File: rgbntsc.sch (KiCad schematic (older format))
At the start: 37 parts, among them J1 VGA, J2 Mini-DIN-4, J3 USB_C_Receptacle_Power, J4 SCART_CONN, U1 SC6206B-65K5, U2 AD724, U8 LM1881, X1 ASE-14.32MHz

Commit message: CXA2075
Replaces AD724 with CXA2075, also adds GBS compatible RGB out header
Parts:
- removed C13, C14: 100n, Capacitor_SMD:C_0805_2012Metric_Pad1.15x1.40mm_HandSolder, symbol Device:C_Small
- removed C3: 1u, Capacitor_SMD:C_0805_2012Metric_Pad1.15x1.40mm_HandSolder, symbol Device:C_Small
- removed C9: 10u, Capacitor_SMD:C_0805_2012Metric_Pad1.15x1.40mm_HandSolder, symbol Device:C_Small
- removed J3: USB_C_Receptacle_Power, videobits:USB_C_Receptacle_Generic_Power_Only, symbol Videobits:USB_C_Receptacle_Power
- removed J4: SCART_CONN, custom_components:SCART_CONN, symbol ossc:SCART_CONN
- removed JP1: Jumper_2_Open, Resistor_SMD:R_0805_2012Metric_Pad1.15x1.40mm_HandSolder, symbol Jumper:Jumper_2_Open
- removed R15, R3: 75, Resistor_SMD:R_0805_2012Metric_Pad1.15x1.40mm_HandSolder, symbol Device:R_Small
- removed R18: 680k, Resistor_SMD:R_0805_2012Metric_Pad1.15x1.40mm_HandSolder, symbol Device:R_Small
- removed R19, R2: 1k, Resistor_SMD:R_0805_2012Metric_Pad1.15x1.40mm_HandSolder, symbol Device:R_Small
- removed U1: SC6206B-65K5, Package_TO_SOT_SMD:SOT-23, symbol Regulator_Linear:MCP1700-2802E_SOT23
- removed U2: AD724, Package_SO:SOIC-16W_7.5x10.3mm_P1.27mm, symbol rgbntsc-rescue:AD724-Videobits
- added C1: 100n, Capacitor_SMD:C_0805_2012Metric_Pad1.15x1.40mm_HandSolder, symbol Device:C_Small
- added C11: 10u, Capacitor_SMD:C_0805_2012Metric_Pad1.15x1.40mm_HandSolder, symbol Device:C_Small
- added C7, C8: 1u, Capacitor_SMD:C_0805_2012Metric_Pad1.15x1.40mm_HandSolder, symbol Device:C_Small
- added J1: USB_C_Receptacle_Power, videobits:USB_C_Receptacle_Generic_Power_Only, symbol Videobits:USB_C_Receptacle_Power
- added J101: Conn_01x08, Connector_JST:JST_XH_B8B-XH-AM_1x08_P2.50mm_Vertical, symbol Connector_Generic:Conn_01x08
- added J3: SCART_CONN, custom_components:SCART_CONN, symbol ossc:SCART_CONN
- added JP101: Jumper_3_Bridged12, Jumper:SolderJumper-3_P1.3mm_Bridged12_Pad1.0x1.5mm, symbol Jumper:Jumper_3_Bridged12
- added R101, R103, R104, R6, R7: 75, Resistor_SMD:R_0805_2012Metric_Pad1.15x1.40mm_HandSolder, symbol Device:R_Small
- added R102, R9: 1k, Resistor_SMD:R_0805_2012Metric_Pad1.15x1.40mm_HandSolder, symbol Device:R_Small
- added R11: 3k3, Resistor_SMD:R_0805_2012Metric_Pad1.15x1.40mm_HandSolder, symbol Device:R_Small
- added R8: 3k, Resistor_SMD:R_0805_2012Metric_Pad1.15x1.40mm_HandSolder, symbol Device:R_Small
- added U102, U103: 74AHCT1G86, Package_TO_SOT_SMD:SOT-23-5, symbol 74xGxx:74AHC1G86
- added U2: SC6206B-65K5, Package_TO_SOT_SMD:SOT-23, symbol Regulator_Linear:MCP1700-2802E_SOT23
- added U3: CXA2075, Package_SO:SOP-24_7.5x15.4mm_P1.27mm, symbol Videobits:CXA2075
- C2: value 1u -> 100n; LCSC C28323 -> C49678
- C3: renamed from C8; LCSC C14663 -> C49678
- C4: renamed from C10; LCSC C14663 -> C49678
- C5: renamed from C4; LCSC C14663 -> C49678
- C9: renamed from C11; LCSC C14663 -> C49678
- R1: value 3k -> 75; LCSC C17513 -> C20638
- R4: value 75 -> 680k; LCSC C20638 -> C17797
- X1: value ASE-14.32MHz -> O32253579545MHEA4SI; LCSC C295523 -> C70606
- renumbered C7 to C10, C1 to C6, J1 to J2, J2 to J4, R5 to R10, R6 to R12, R7 to R13, R8 to R14, R16 to R2, R17 to R3, U8 to U1
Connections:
- net labels added: STRIP_CSYNC, SYNC, VGA_CSYNC
- wire segments 113 -> 146

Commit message: added 1v amp and output caps
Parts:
- removed J101: Conn_01x08, Connector_JST:JST_XH_B8B-XH-AM_1x08_P2.50mm_Vertical, symbol Connector_Generic:Conn_01x08
- removed R101, R103, R104: 75, Resistor_SMD:R_0805_2012Metric_Pad1.15x1.40mm_HandSolder, symbol Device:R_Small
- added C12, C13, C14: 220u, Capacitor_SMD:CP_Elec_6.3x5.4, symbol Device:CP_Small
- added C15, C16, C17: 1u, Capacitor_SMD:C_0805_2012Metric, symbol rgbntsc-rescue:C_Small-Device
- added R15, R16, R17: 180, Resistor_SMD:R_0805_2012Metric, symbol rgbntsc-rescue:R_Small-Device
- added R18, R19, R20: 75, Resistor_SMD:R_0805_2012Metric, symbol rgbntsc-rescue:R_Small-Device
- added U6: TPF144-VR, Package_SO:MSOP-10_3x3mm_P0.5mm, symbol Videobits:TPF144-VR
- C1, C2, C3, C4: footprint Capacitor_SMD:C_0805_2012Metric_Pad1.15x1.40mm_HandSolder -> Capacitor_SMD:C_0805_2012Metric; symbol Device:C_Small -> rgbntsc-rescue:C_Small-Device
- C10: renamed from C11; footprint Capacitor_SMD:C_0805_2012Metric_Pad1.15x1.40mm_HandSolder -> Capacitor_SMD:C_0805_2012Metric; symbol Device:C_Small -> rgbntsc-rescue:C_Small-Device
- C11: renamed from C5; footprint Capacitor_SMD:C_0805_2012Metric_Pad1.15x1.40mm_HandSolder -> Capacitor_SMD:C_0805_2012Metric; symbol Device:C_Small -> rgbntsc-rescue:C_Small-Device
- C5: renamed from C6; footprint Capacitor_SMD:C_0805_2012Metric_Pad1.15x1.40mm_HandSolder -> Capacitor_SMD:C_0805_2012Metric; symbol Device:C_Small -> rgbntsc-rescue:C_Small-Device
- C6: renamed from C7; footprint Capacitor_SMD:C_0805_2012Metric_Pad1.15x1.40mm_HandSolder -> Capacitor_SMD:C_0805_2012Metric; symbol Device:C_Small -> rgbntsc-rescue:C_Small-Device
- C7: renamed from C8; footprint Capacitor_SMD:C_0805_2012Metric_Pad1.15x1.40mm_HandSolder -> Capacitor_SMD:C_0805_2012Metric; symbol Device:C_Small -> rgbntsc-rescue:C_Small-Device
- C8: renamed from C9; footprint Capacitor_SMD:C_0805_2012Metric_Pad1.15x1.40mm_HandSolder -> Capacitor_SMD:C_0805_2012Metric; symbol Device:C_Small -> rgbntsc-rescue:C_Small-Device
- C9: renamed from C10; symbol Device:CP_Small -> rgbntsc-rescue:CP_Small-Device
- GOTE1: symbol Mechanical:Fiducial -> rgbntsc-rescue:Fiducial-Mechanical
- J4: symbol Connector:Mini-DIN-4 -> rgbntsc-rescue:Mini-DIN-4-Connector
- JP1: renamed from JP101; symbol Jumper:Jumper_3_Bridged12 -> rgbntsc-rescue:Jumper_3_Bridged12-Jumper
- JR1, JR2, JU1: symbol Connector:Conn_Coaxial -> rgbntsc-rescue:Conn_Coaxial-Connector
- R1, R10, R11, R12, R13, R14, R2, R3, R4, R6, R7: footprint Resistor_SMD:R_0805_2012Metric_Pad1.15x1.40mm_HandSolder -> Resistor_SMD:R_0805_2012Metric; symbol Device:R_Small -> rgbntsc-rescue:R_Small-Device
- R5: renamed from R102; footprint Resistor_SMD:R_0805_2012Metric_Pad1.15x1.40mm_HandSolder -> Resistor_SMD:R_0805_2012Metric; symbol Device:R_Small -> rgbntsc-rescue:R_Small-Device
- R8: value 3k -> 1k; footprint Resistor_SMD:R_0805_2012Metric_Pad1.15x1.40mm_HandSolder -> Resistor_SMD:R_0805_2012Metric; symbol Device:R_Small -> rgbntsc-rescue:R_Small-Device
- R9: value 1k -> 1k3; footprint Resistor_SMD:R_0805_2012Metric_Pad1.15x1.40mm_HandSolder -> Resistor_SMD:R_0805_2012Metric; symbol Device:R_Small -> rgbntsc-rescue:R_Small-Device
- U1: symbol Video:LM1881 -> rgbntsc-rescue:LM1881-Video
- U2: renamed from U102; symbol 74xGxx:74AHC1G86 -> rgbntsc-rescue:74AHC1G86-74xGxx
- U3: renamed from U103; symbol 74xGxx:74AHC1G86 -> rgbntsc-rescue:74AHC1G86-74xGxx
- U4: renamed from U2; symbol Regulator_Linear:MCP1700-2802E_SOT23 -> rgbntsc-rescue:MCP1700-2802E_SOT23-Regulator_Linear
- U5: renamed from U3; footprint Package_SO:SOP-24_7.5x15.4mm_P1.27mm -> Package_SO:SO-24_5.3x15mm_P1.27mm
- X1: symbol Oscillator:ASE-xxxMHz -> rgbntsc-rescue:ASE-xxxMHz-Oscillator
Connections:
- wire segments 146 -> 162
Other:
- moved on the sheet: U5

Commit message: corrected components
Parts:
- C12, C13, C14, U5: LCSC (none) -> NOT FITTED
- R15, R16, R17: LCSC C20638 -> C25270
- R9: LCSC C17513 -> C17384
- U6: LCSC (none) -> C155447
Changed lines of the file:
@@
 F 2 "Resistor_SMD:R_0805_2012Metric" H 5250 6750 50  0001 C CNN
 F 3 "~" H 5250 6750 50  0001 C CNN
-F 4 "C17513" H 5250 6750 50  0001 C CNN "LCSC"
+F 4 "C17384" H 5250 6750 50  0001 C CNN "LCSC"
 	1    5250 6750
 	1    0    0    -1
@@
 F 2 "Package_SO:SO-24_5.3x15mm_P1.27mm" H 7850 2000 60  0001 C CNN
 F 3 "" H 7850 2000 60  0000 C CNN
+F 4 "NOT FITTED" H 7850 2000 50  0001 C CNN "LCSC"
 	1    7850 2000
 	1    0    0    -1
@@
 F 2 "Capacitor_SMD:CP_Elec_6.3x5.4" H 9600 2100 50  0001 C CNN
 F 3 "~" H 9600 2100 50  0001 C CNN
+F 4 "NOT FITTED" H 9600 2100 50  0001 C CNN "LCSC"
 	1    9600 2100
 	0    -1   1    0
@@
 F 2 "Capacitor_SMD:CP_Elec_6.3x5.4" H 9600 2000 50  0001 C CNN
 F 3 "~" H 9600 2000 50  0001 C CNN
+F 4 "NOT FITTED" H 9600 2000 50  0001 C CNN "LCSC"
 	1    9600 2000
 	0    -1   1    0
@@
 F 2 "Capacitor_SMD:CP_Elec_6.3x5.4" H 9600 1900 50  0001 C CNN
 F 3 "~" H 9600 1900 50  0001 C CNN
+F 4 "NOT FITTED" H 9600 1900 50  0001 C CNN "LCSC"
 	1    9600 1900
 	0    -1   1    0
@@
 F 2 "Package_SO:MSOP-10_3x3mm_P0.5mm" H 5475 2797 60  0000 C CNN
 F 3 "" H 5250 2400 60  0000 C CNN
+F 4 "C155447" H 5450 2150 50  0001 C CNN "LCSC"
 	1    5450 2150
 	1    0    0    -1
@@
 F 2 "Resistor_SMD:R_0805_2012Metric" H 7150 2350 50  0001 C CNN
 F 3 "~" H 7150 2350 50  0001 C CNN
-F 4 "C20638" H 7150 2350 50  0001 C CNN "LCSC"
+F 4 "C25270" H 7150 2350 50  0001 C CNN "LCSC"
 	1    7150 2350
 	1    0    0    -1
@@
 F 2 "Resistor_SMD:R_0805_2012Metric" H 7050 2350 50  0001 C CNN
 F 3 "~" H 7050 2350 50  0001 C CNN
-F 4 "C20638" H 7050 2350 50  0001 C CNN "LCSC"
+F 4 "C25270" H 7050 2350 50  0001 C CNN "LCSC"
 	1    7050 2350
 	1    0    0    -1
@@
 F 2 "Resistor_SMD:R_0805_2012Metric" H 6950 2350 50  0001 C CNN
 F 3 "~" H 6950 2350 50  0001 C CNN
-F 4 "C20638" H 6950 2350 50  0001 C CNN "LCSC"
+F 4 "C25270" H 6950 2350 50  0001 C CNN "LCSC"
 	1    6950 2350
 	1    0    0    -1

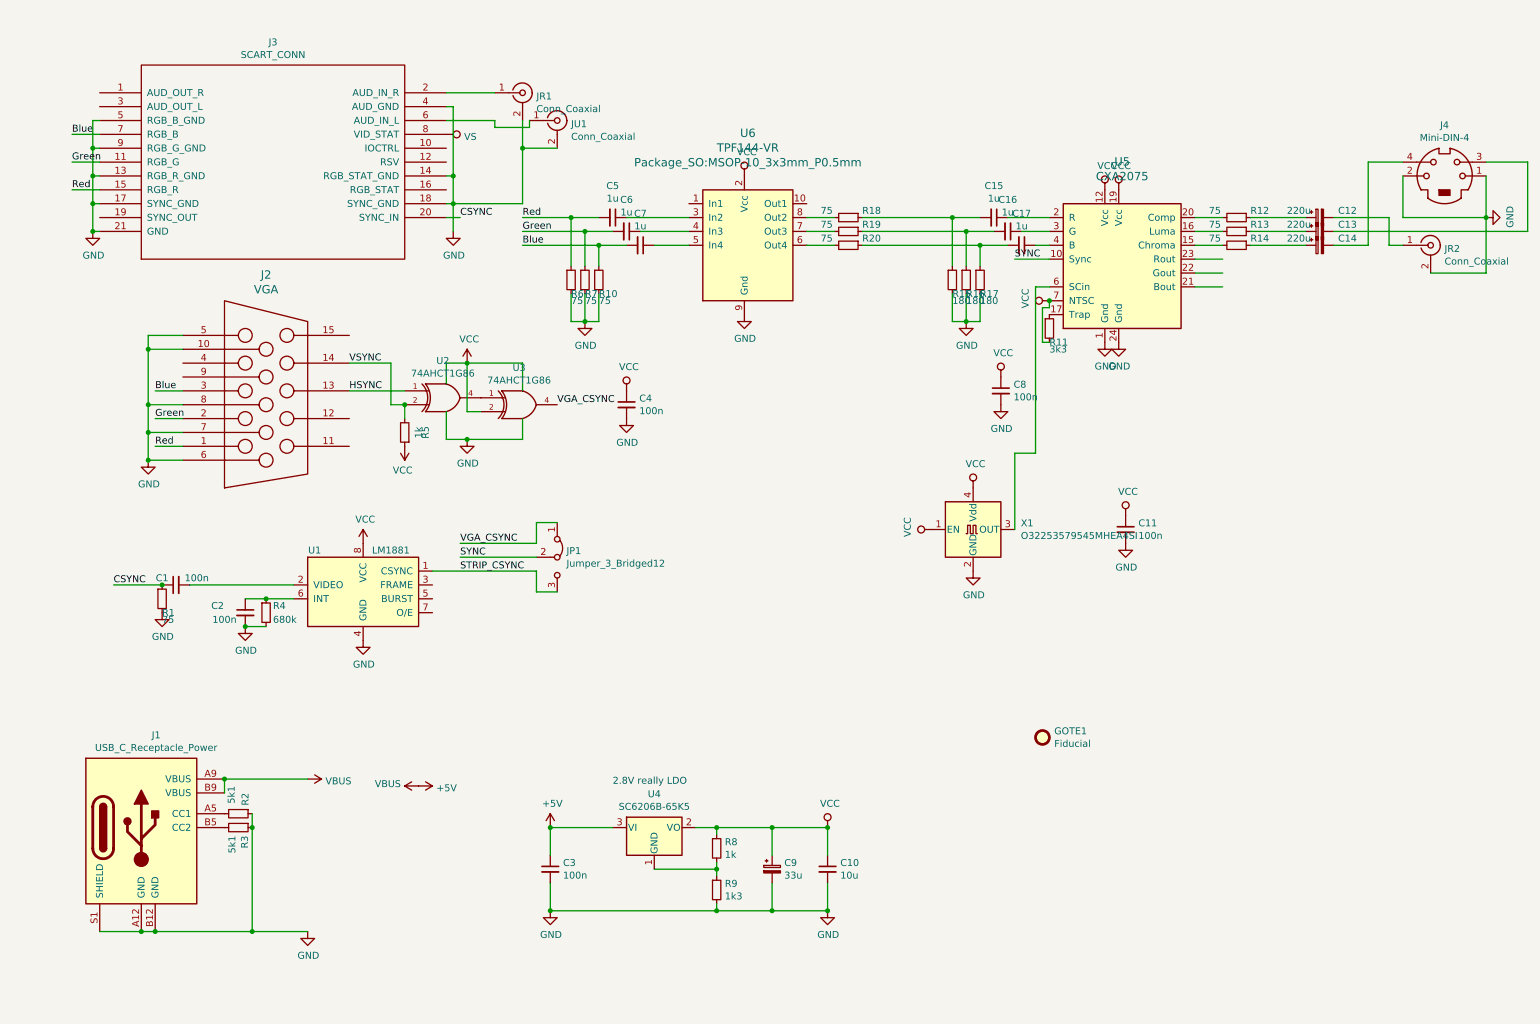
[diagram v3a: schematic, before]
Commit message: add power LED, general tweakage
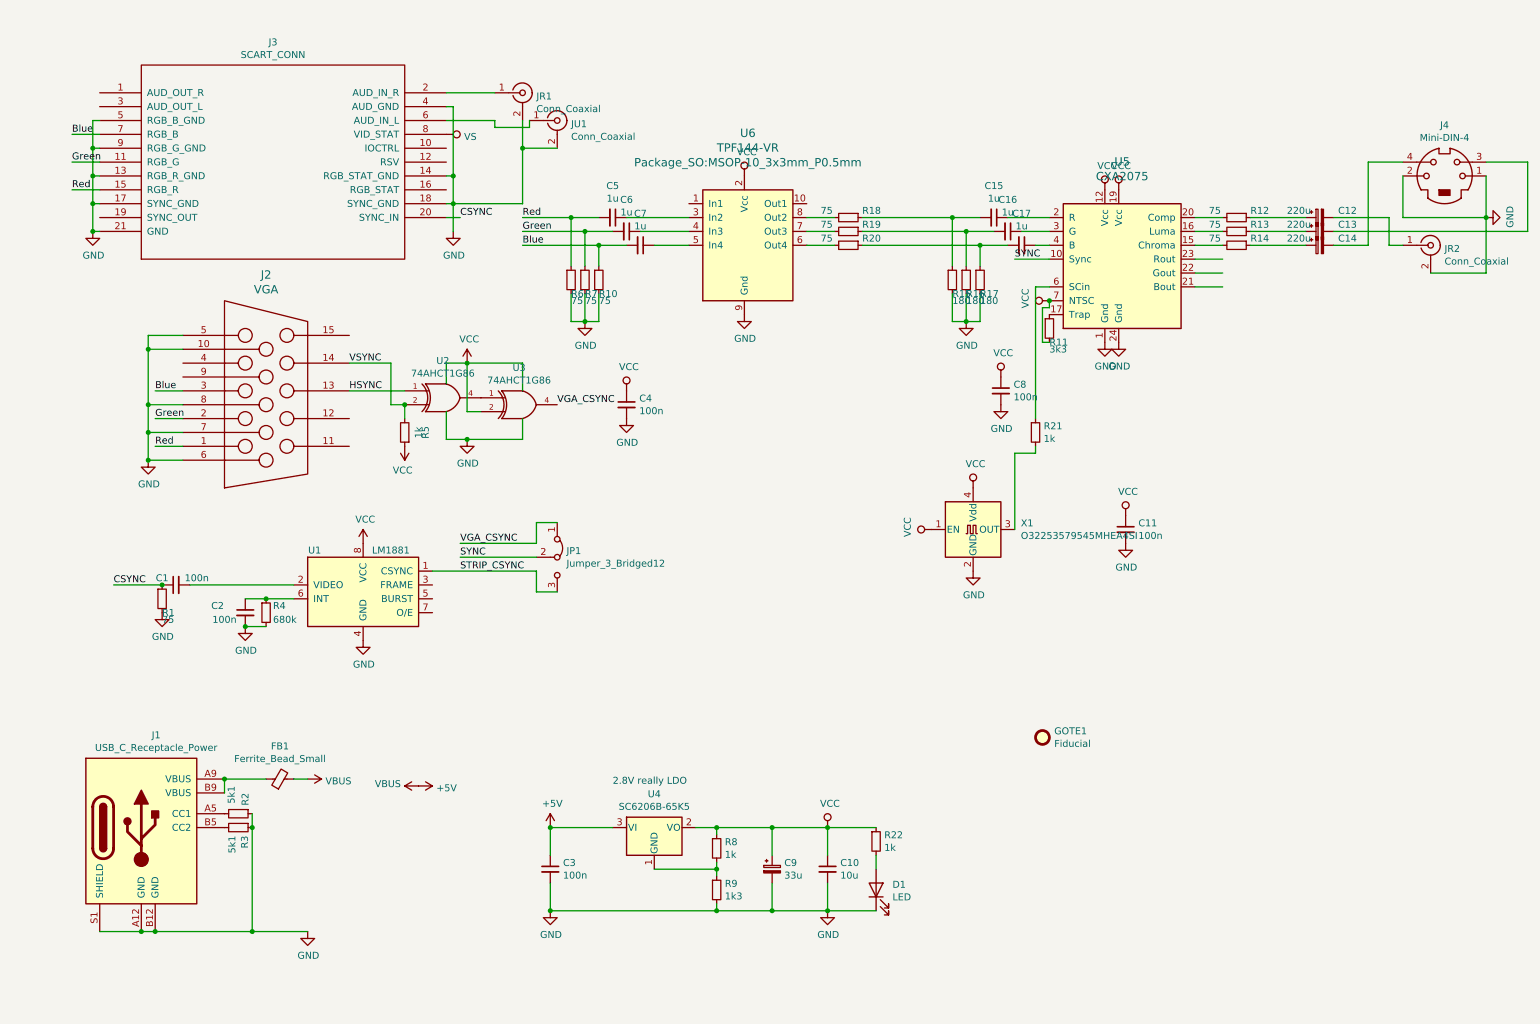
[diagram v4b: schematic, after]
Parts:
- added D1: LED, LED_SMD:LED_0805_2012Metric, symbol Device:LED
- added FB1: Ferrite_Bead_Small, Capacitor_SMD:C_0805_2012Metric, symbol Device:Ferrite_Bead_Small
- added R21, R22: 1k, Resistor_SMD:R_0805_2012Metric, symbol rgbntsc-rescue:R_Small-Device
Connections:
- net +5V: now also FB1.2; no longer J1.A9 (VBUS), J1.B9 (VBUS)
- net GND: now also D1.1 (K)
- net VCC: now also R22.1
- net at X1.3 (OUT): now also R21.2; no longer U5.6 (SCin)
- new net: R21.1, U5.6 (SCin)
- new net: FB1.1, J1.A9 (VBUS), J1.B9 (VBUS)
- new net: D1.2 (A), R22.2
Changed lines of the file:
@@
 	1700 6050 1700 5950
 Wire Wire Line
-	1700 5950 2300 5950
+	1700 5950 2000 5950
 Connection ~ 1700 5950
 $Comp
@@
 	7400 3600 7550 3600
 Wire Wire Line
-	7550 3600 7550 2400
+	7550 3600 7550 3550
 Wire Wire Line
 	7550 2400 7650 2400
@@
 Wire Wire Line
 	7650 2100 7550 2100
+$Comp
+L rgbntsc-rescue:R_Small-Device R21
+U 1 1 60AAAD05
+P 7550 3450
+F 0 "R21" H 7609 3496 50  0000 L CNN
+F 1 "1k" H 7609 3405 50  0000 L CNN
+F 2 "Resistor_SMD:R_0805_2012Metric" H 7550 3450 50  0001 C CNN
+F 3 "~" H 7550 3450 50  0001 C CNN
+F 4 "C17513" H 7550 3450 50  0001 C CNN "LCSC"
+	1    7550 3450
+	1    0    0    -1
+$EndComp
+Wire Wire Line
+	7550 3350 7550 2400
+$Comp
+L Device:Ferrite_Bead_Small FB1
+U 1 1 60AAC928
+P 2100 5950
+F 0 "FB1" V 2337 5950 50  0000 C CNN
+F 1 "Ferrite_Bead_Small" V 2246 5950 50  0000 C CNN
+F 2 "Capacitor_SMD:C_0805_2012Metric" V 2030 5950 50  0001 C CNN
+F 3 "~" H 2100 5950 50  0001 C CNN
+F 4 "C1017" V 2100 5950 50  0001 C CNN "LCSC"
+	1    2100 5950
+	0    -1   -1   0
+$EndComp
+Wire Wire Line
+	2200 5950 2300 5950
+$Comp
+L rgbntsc-rescue:R_Small-Device R22
+U 1 1 60C1454C
+P 6400 6400
+F 0 "R22" H 6459 6446 50  0000 L CNN
+F 1 "1k" H 6459 6355 50  0000 L CNN
+F 2 "Resistor_SMD:R_0805_2012Metric" H 6400 6400 50  0001 C CNN
+F 3 "~" H 6400 6400 50  0001 C CNN
+F 4 "C17513" H 6400 6400 50  0001 C CNN "LCSC"
+	1    6400 6400
+	1    0    0    -1
+$EndComp
+$Comp
+L Device:LED D1
+U 1 1 60C1D817
+P 6400 6750
+F 0 "D1" V 6439 6632 50  0000 R CNN
+F 1 "LED" V 6348 6632 50  0000 R CNN
+F 2 "LED_SMD:LED_0805_2012Metric" H 6400 6750 50  0001 C CNN
+F 3 "~" H 6400 6750 50  0001 C CNN
+F 4 "C34499" V 6400 6750 50  0001 C CNN "LCSC"
+	1    6400 6750
+	0    -1   -1   0
+$EndComp
+Wire Wire Line
+	6400 6900 6050 6900
+Wire Wire Line
+	6400 6500 6400 6600
+Wire Wire Line
+	6400 6300 6050 6300
 $EndSCHEMATC

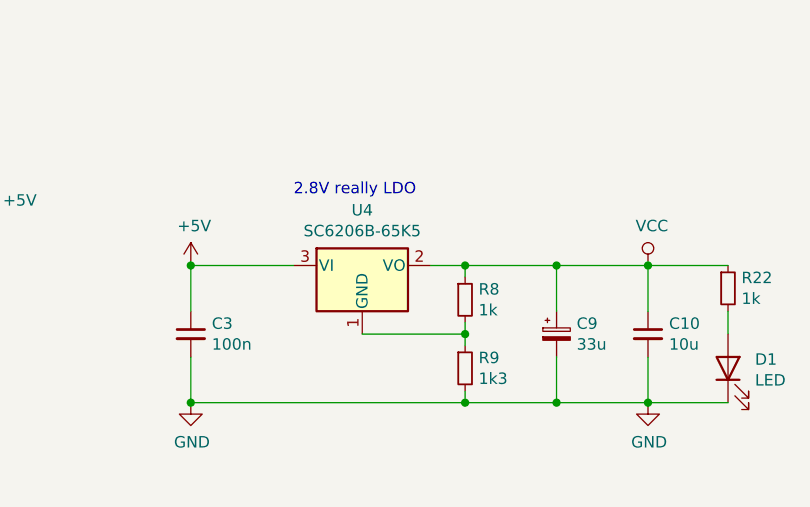
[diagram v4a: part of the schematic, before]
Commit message: fix regulator resistor, add schematic pdf
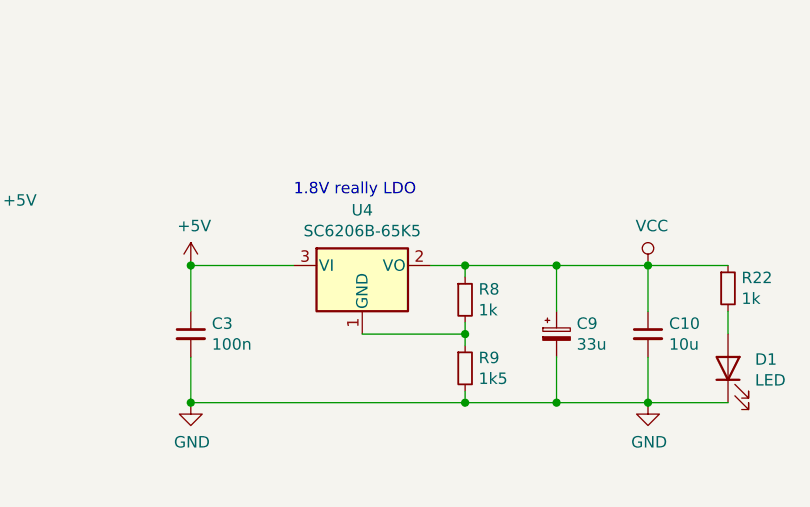
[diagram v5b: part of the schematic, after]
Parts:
- R9: value 1k3 -> 1k5; LCSC C17384 -> C4310
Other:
- note added: "1.8V really LDO"
- note removed: "2.8V really LDO"
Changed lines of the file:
@@
 P 5250 6750
 F 0 "R9" H 5309 6796 50  0000 L CNN
-F 1 "1k3" H 5309 6705 50  0000 L CNN
+F 1 "1k5" H 5309 6705 50  0000 L CNN
 F 2 "Resistor_SMD:R_0805_2012Metric" H 5250 6750 50  0001 C CNN
 F 3 "~" H 5250 6750 50  0001 C CNN
-F 4 "C17384" H 5250 6750 50  0001 C CNN "LCSC"
+F 4 "C4310" H 5250 6750 50  0001 C CNN "LCSC"
 	1    5250 6750
 	1    0    0    -1
@@
 $EndComp
 Text Notes 4500 6000 0    50   ~ 0
-2.8V really LDO
+1.8V really LDO
 Wire Wire Line
 	4600 1900 5050 1900
